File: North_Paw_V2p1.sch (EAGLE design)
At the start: 19 parts, among them Q1 8MHz

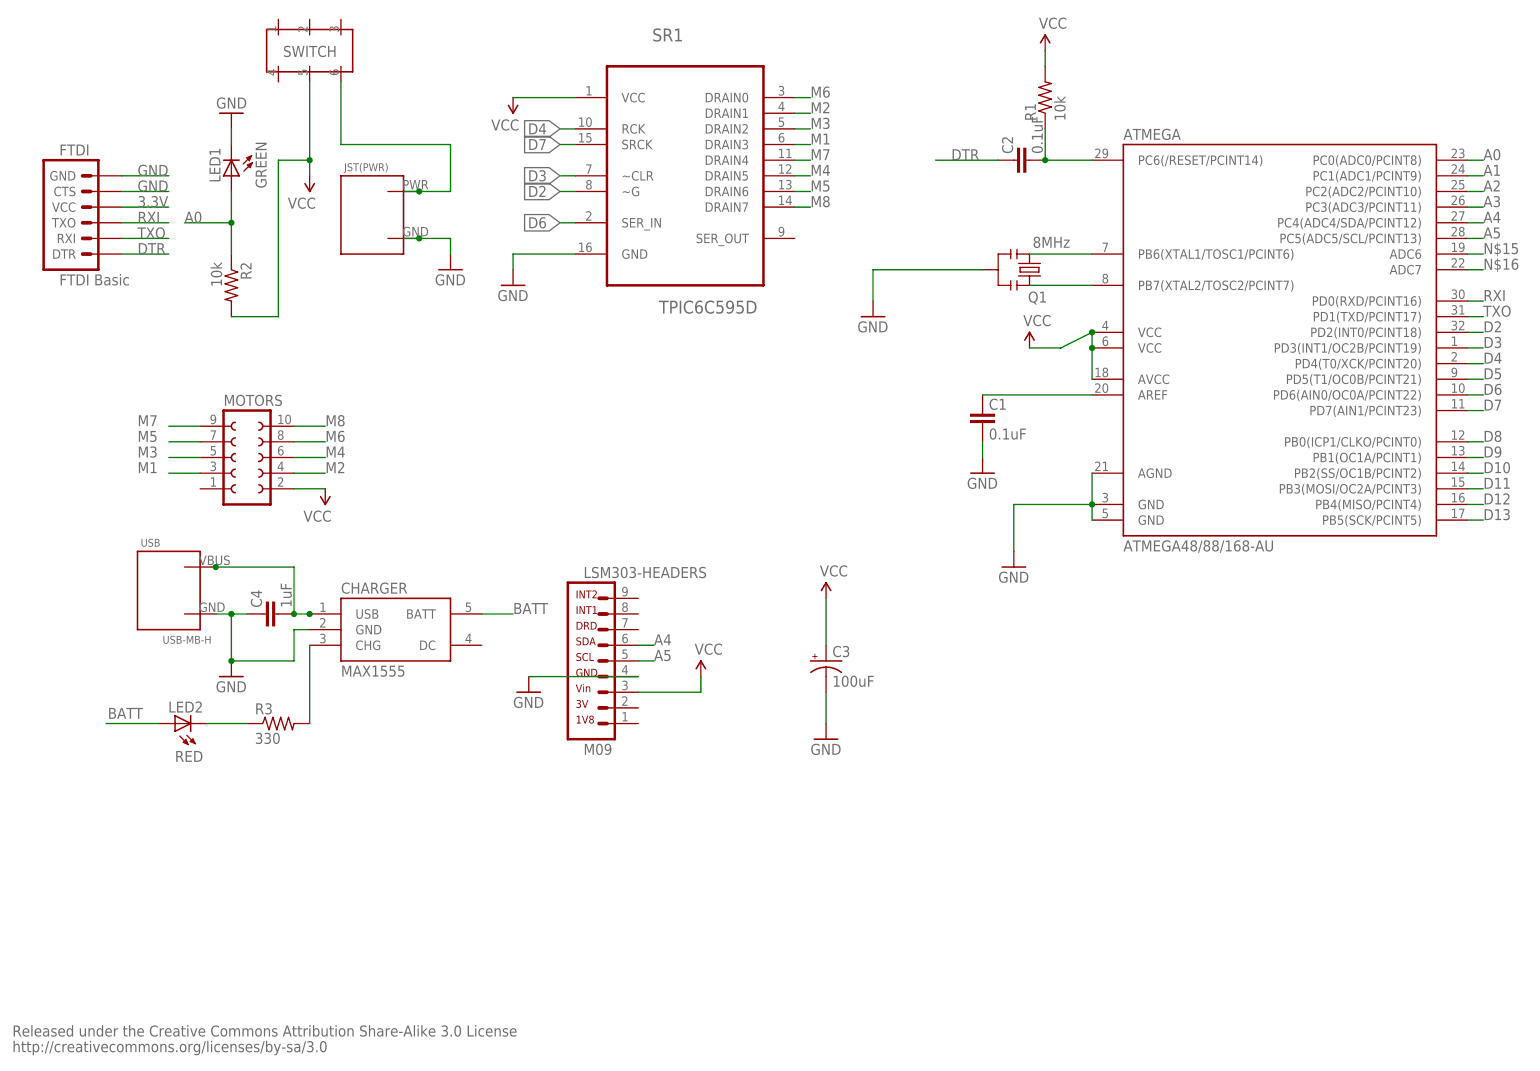
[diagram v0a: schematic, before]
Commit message: More smd and routing updates
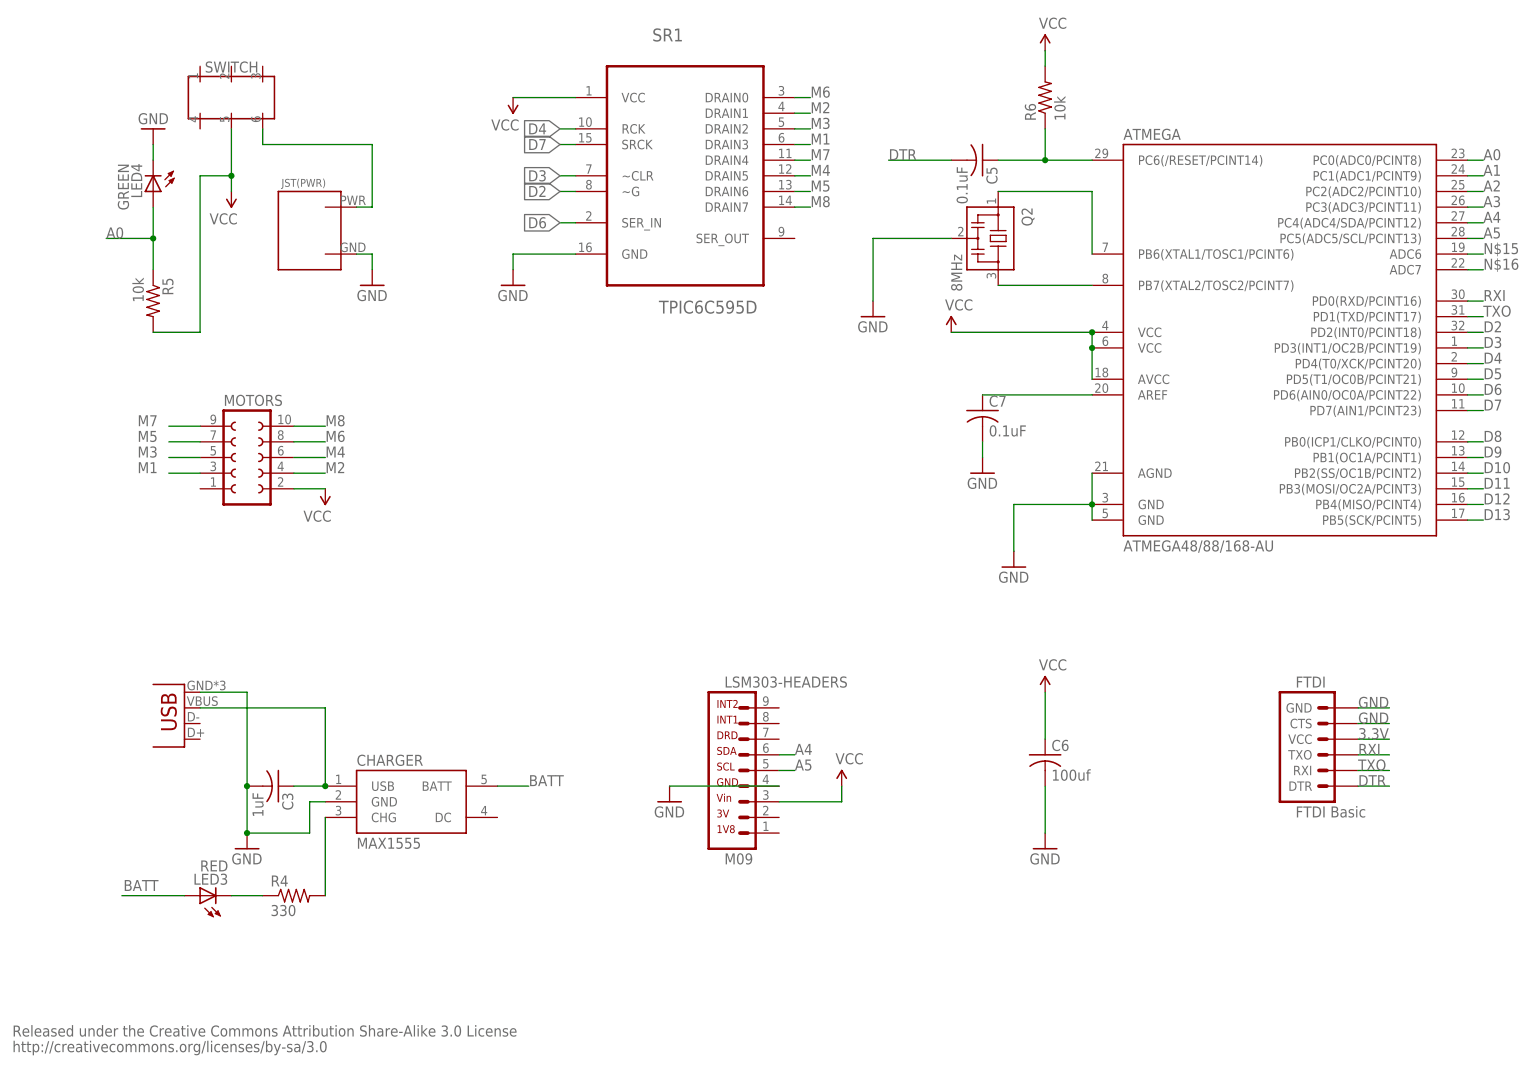
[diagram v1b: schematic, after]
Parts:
- removed C1, C2: 0.1uF, SparkFun:CAPPTH
- removed C4: 1uF, SparkFun:CAPPTH
- removed LED1: GREEN, SparkFun:LED3MM
- removed LED2: RED, SparkFun:LED3MM
- removed Q1: 8MHz, SparkFun:RESONATORPTH
- removed R1: 10k, resistor:R-US_0204/5
- removed R2: 10k, resistor:R-US_0204/7
- removed R3: 330, resistor:R-US_0204/7
- removed USB: USB-MB-H, North_Paw:USB-MB-H
- added C5, C7: 0.1uF, adafruit:C-USC0805
- added C6: 100uf, adafruit:C-USC0805
- added JP1: USB-MICROB, SparkFun-Connectors:USB-MICROB
- added LED3: RED, adafruit:LEDCHIP-LED0805
- added LED4: GREEN, adafruit:LEDCHIP-LED0805
- added Q2: 8MHz, murata-filter:CSTCR6M00G53Z
- added R4: 330, adafruit:R-US_R0805
- added R5, R6: 10k, adafruit:R-US_R0805
- C3: value 100uF -> 1uF; device SparkFun:CAP_POLPTH1 -> adafruit:C-USC0805
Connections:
- removed net N$9: LED2.C, R3.1
- new net N$8: LED3.C, R4.1
- net 3.3V: now also C6.1, R5.2, R6.2; no longer C3.+, R1.2, R2.2
- net A0: now also LED4.A, R5.1; no longer LED1.A, R2.1
- net BATT: now also LED3.A; no longer LED2.A
- net DTR: now also C5.2; no longer C2.2
- net GND: now also C3.2, C6.2, C7.2, JP1.GND, LED4.C, Q2.2; no longer C1.1, C3.-, C4.2, LED1.C, Q1.2, USB.GND
- net N$1: now also Q2.1; no longer Q1.3
- net N$2: now also Q2.3; no longer Q1.1
- net N$3: now also C7.1; no longer C1.2
- net N$7: now also R4.2; no longer R3.2
- net RESET: now also C5.1, R6.1; no longer C2.1, R1.1
- net USB_VIN: now also C3.1, JP1.VBUS; no longer C4.1, USB.PWR
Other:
- moved on the sheet: CHARGER, FTDI, JST(PWR), LSM303-HEADERS

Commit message: Initial checkin of TopoR
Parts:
- removed SWITCH: OS202011MA0QS1, OS202011MA0QS1:OS202011MA0QS1
- added S1: (no value), SparkFun-Electromechanical:SWITCH-SPDT-SMD-A
- ATMEGA, FTDI, JP1, JST(PWR), LSM303-HEADERS, MOTORS: OC_NEWARK (none) -> unknown
- C3: MF (none) -> KEMET; MPN (none) -> C0805C105K4RACTU; OC_NEWARK (none) -> 70K9137
- C5, C7: MPN (none) -> C0805C104K3RACTU; OC_NEWARK (none) -> 54K3711
- C6: MPN (none) -> TLCR107M004XTA; OC_NEWARK (none) -> 59M9595
- CHARGER: MPN (none) -> MAX1555EZK+T.; OC_NEWARK (none) -> 26R6103
- LED3: MPN (none) -> 150080RS75000; OC_NEWARK (none) -> 95W3801
- LED4: MPN (none) -> 150080GS75000; OC_NEWARK (none) -> 95W3800
- R4: MPN (none) -> CRCW0805330RJNEA; OC_NEWARK (none) -> 59M6894
- R5, R6: MF (none) -> VISHAY/DALE; MPN (none) -> CRCW080510K0FKTA; OC_NEWARK (none) -> 05F1511
- SR1: MF (none) -> TEXAS INSTRUMENTS
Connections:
- new net N$4: JST(PWR).PWR, S1.S
- net 3.3V: now also S1.P; no longer SWITCH.5
- net BATT: no longer JST(PWR).PWR, SWITCH.6
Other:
- note removed: "SWITCH"
